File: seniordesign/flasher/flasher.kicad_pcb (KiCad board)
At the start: 2 copper layers, 17 parts, among them IC1 ATTINY24-SS, P1 PROG_PINS, P2 GPIO, P3 OUT, Q1 BC847S, Q2 BC847S

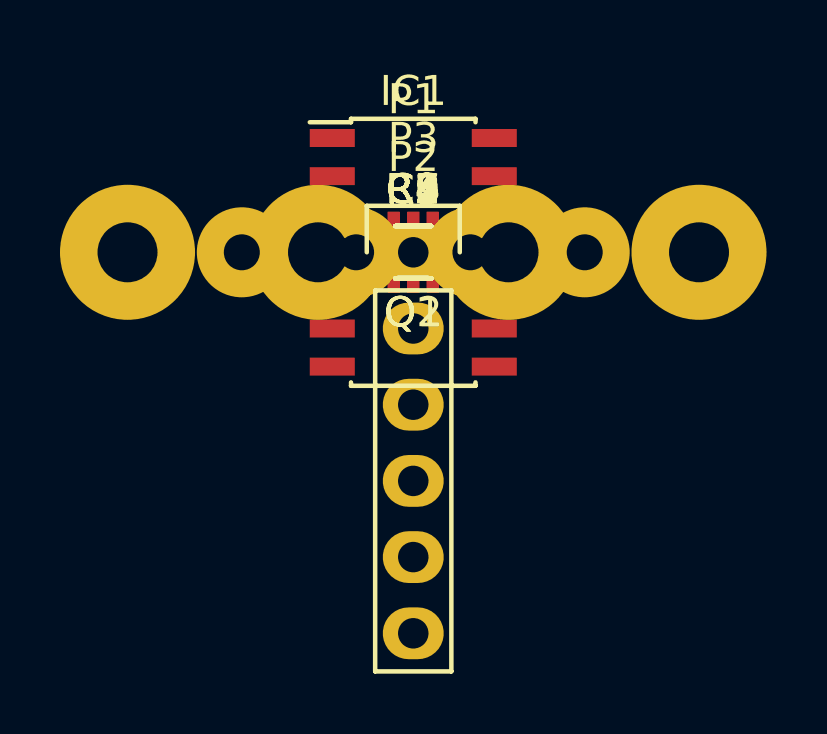
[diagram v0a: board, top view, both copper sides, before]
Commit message: Fix flasher; now generates footprints successfully!
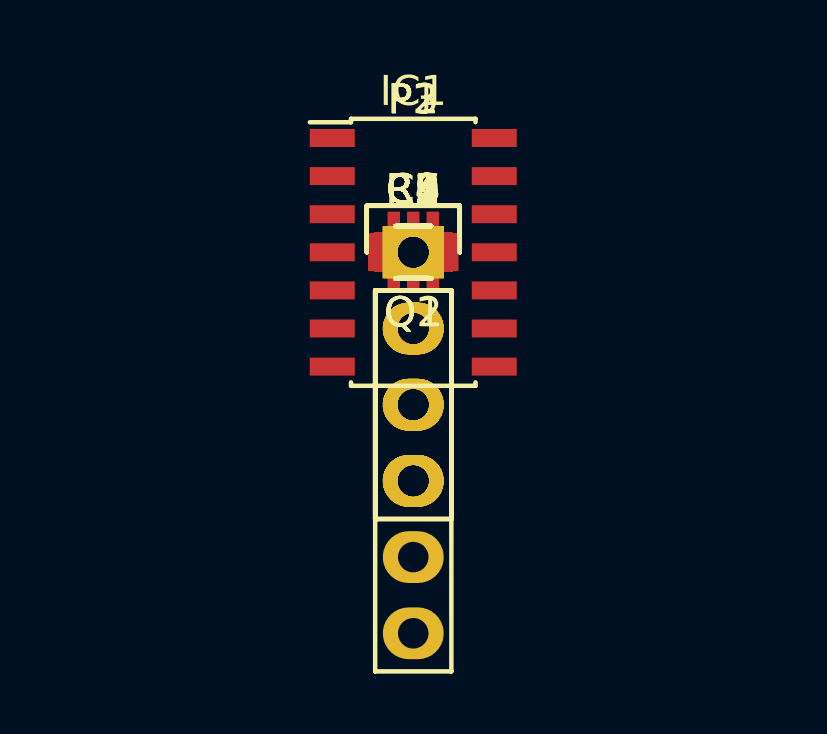
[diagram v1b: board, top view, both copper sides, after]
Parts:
- P2: footprint Wire_Pads:SolderWirePad_4xInline_1-2mmDrill -> Pin_Headers:Pin_Header_Straight_1x04
- P3: footprint Wire_Pads:SolderWirePad_4xInline_2mmDrill -> Pin_Headers:Pin_Header_Straight_1x04
